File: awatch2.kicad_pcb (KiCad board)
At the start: 4 copper layers, 102.4 x 46.1 mm, 167 parts, among them J101 Conn_01x02, J102 Conn_01x02, J103 Conn_01x02, J104 Conn_01x02, J301 Conn_01x02, J801 Molex 1050170001, J802 Conn_01x06, Q701 FDV301N, SW101 B3S-1000, SW102 B3S-1000, SW103 B3S-1000, SW104 B3S-1000, U1 nRF52840, U301 MAX14690, U401 W25Q128JVPIQTR, U501 BMM150, U502 APDS-9306-065, U503 BMI160, U504 BMP388, U601 SPK0641HT4H-1, U701 AYF531035 (LS013B7DH05), U801 AT93C46DN-SH-T, U802 MCP1703A-3302_SOT223, U803 FT2232HL, U901 DRV2604, X1 ABM11W-32.0000MHZ-8-B1U-T3, Y801 FH1200004

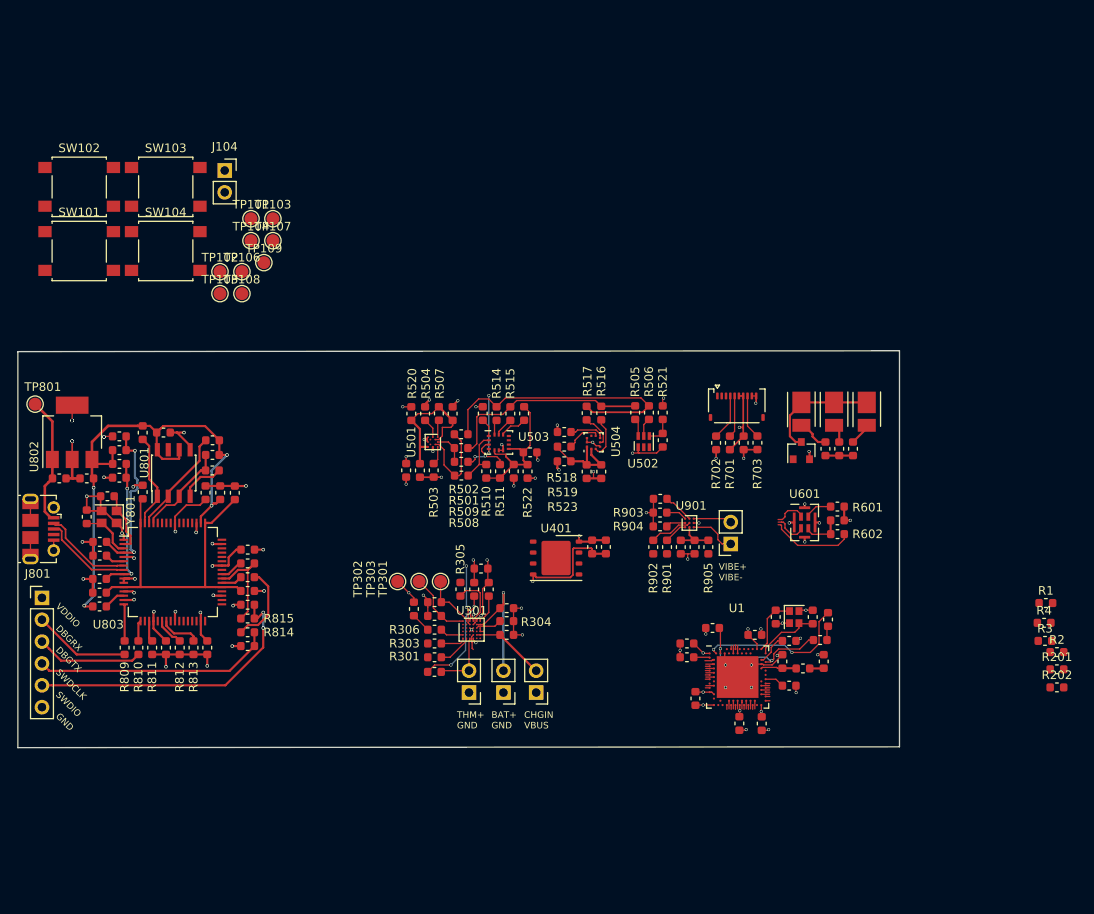
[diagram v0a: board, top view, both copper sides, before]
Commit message: place PMIC and vibrate driver
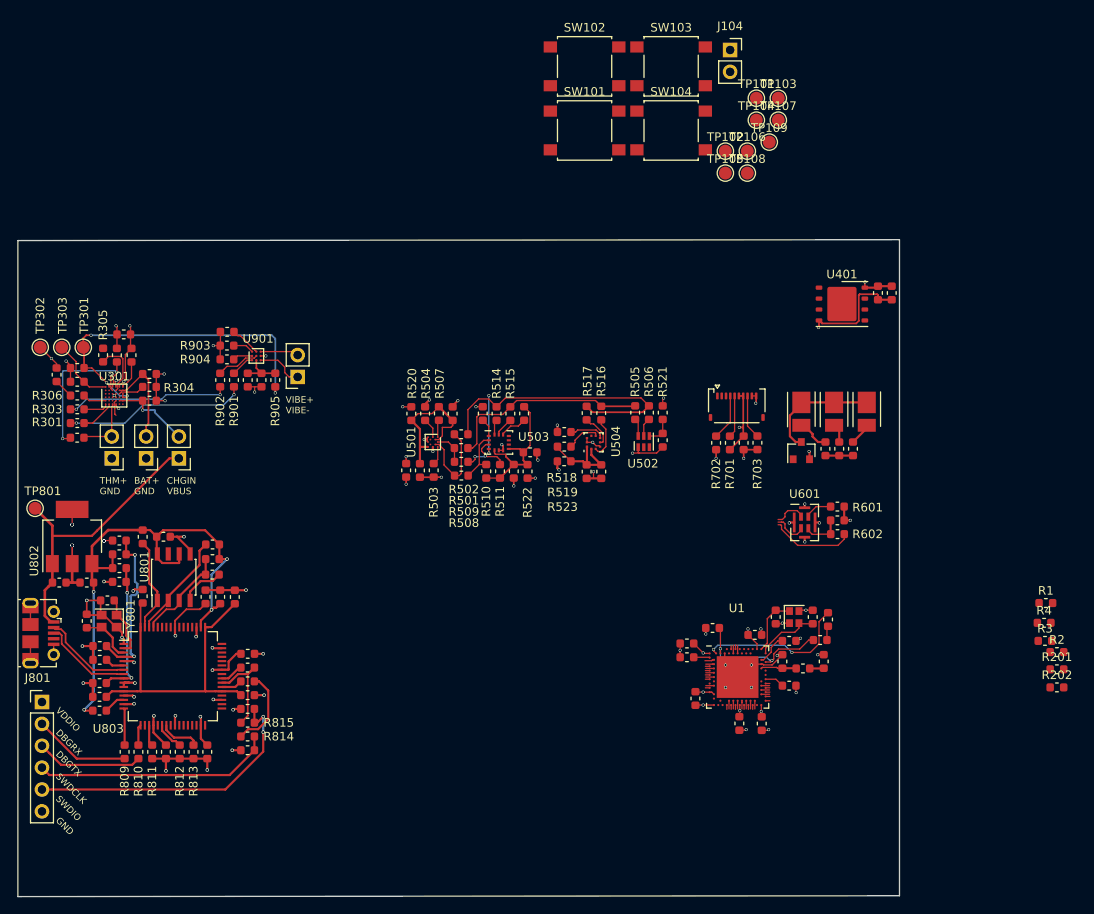
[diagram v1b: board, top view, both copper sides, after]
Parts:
- moved J104 60.3 mm to (126.7, 2.97)
- moved SW101 60.3 mm to (109.8, 12.3)
- moved SW102 60.3 mm to (109.8, 4.87)
- moved TP101 60.3 mm to (129.8, 8.57)
- moved TP104 60.3 mm to (129.8, 11.1)
- moved TP109 60.3 mm to (131.3, 13.7)
- moved SW103 60.3 mm to (119.9, 4.87)
- moved SW104 60.3 mm to (119.9, 12.3)
- moved TP102 60.3 mm to (126.2, 14.7)
- moved TP103 60.3 mm to (132.3, 8.57)
- moved TP105 60.3 mm to (126.2, 17.3)
- moved TP106 60.3 mm to (128.7, 14.7)
- moved TP107 60.3 mm to (132.3, 11.1)
- moved TP108 60.3 mm to (128.7, 17.3)
- moved R901 53.9 mm to (69.1, 41.3)
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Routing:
- net +3V8: track 7.18 -> 41.1 mm, vias 0 -> 4
- net /PMIC/PMIC_SCL: track 0.50 -> 21.8 mm, vias 0 -> 2
- net /PMIC/PMIC_SDA: track 0.95 -> 20.0 mm, vias 0 -> 2
- net VBUS: track 15.0 -> 33.4 mm
- net /PMIC/PMIC_INTn: track 7.92 -> 2.93 mm, vias 2 -> 1
- net /PMIC/MAX_CAP: track 14.1 -> 18.3 mm
- net /PMIC/BAT+: track 14.5 -> 11.7 mm, vias 1 -> 0
- net /PMIC/MAX_CHGIN: track 8.62 -> 9.46 mm, vias 0 -> 2
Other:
- board size 102.4 x 46.1 mm -> 102.4 x 76.3 mm
- net class Magnetometer 4/4: clearance 0.1016 -> 0.127
- net class NRF 3/3: clearance 0.1016 -> 0.127
- net class Vibe 2.75: clearance 0.0762 -> 0.127

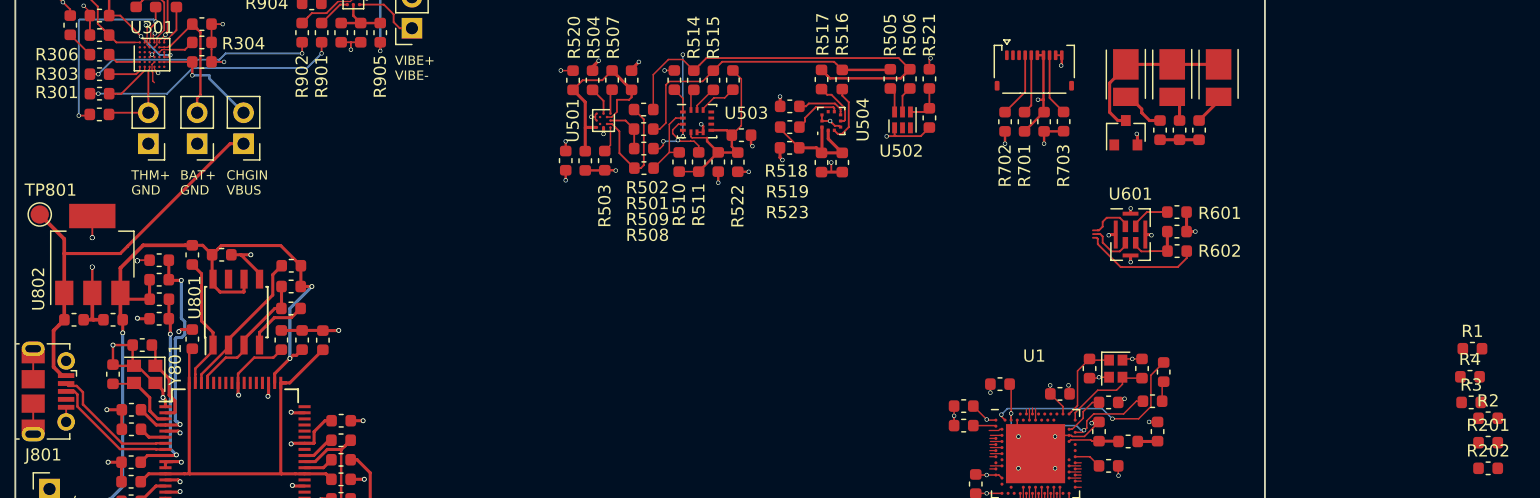
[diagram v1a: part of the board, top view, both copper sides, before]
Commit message: place PMIC I2C pullups
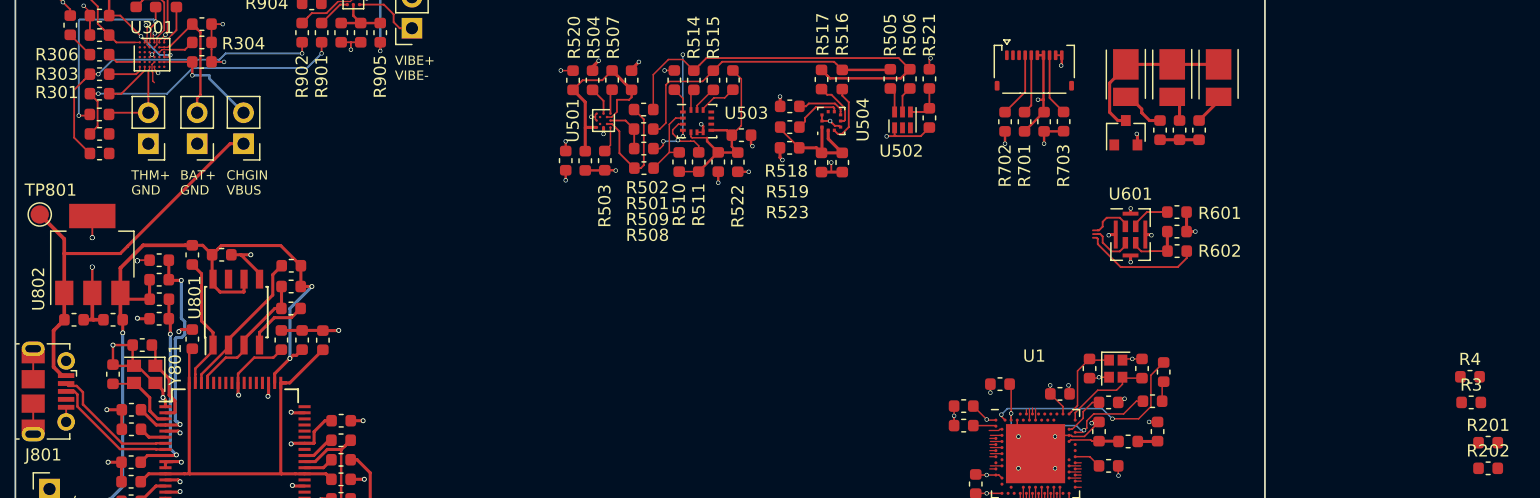
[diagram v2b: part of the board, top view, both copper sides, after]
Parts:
- moved R2 115.8 mm to (50.9, 51.2), turned to 180 degrees
- moved R1 113.9 mm to (50.9, 49.6), turned to 180 degrees
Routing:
- net /PMIC/PMIC_SDA: track 20.0 -> 27.5 mm
- net /PMIC/PMIC_SCL: track 21.8 -> 25.6 mm
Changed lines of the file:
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@@
     (thickness 1.6)
     (drawings 14)
-    (tracks 1100)
+    (tracks 1108)
     (zones 0)
     (modules 167)
@@
   )
   (module Resistor_SMD:R_0603_1608Metric (layer F.Cu)
-    (at 164.6875 72.9)
+    (at 50.9 51.2 180)
     (descr "Resistor SMD 0603 (1608 Metric), square (rectangular) end terminal, IPC_7351 nominal, (Body size source: http://www.tortai-tech.com/upload/download/2011102023233369053.pdf), generated with kicad-footprint-generator")
     (tags resistor)
     (attr smd)
-    (fp_text reference R2 (at 0 -1.43) (layer F.SilkS)
+    (fp_text reference R2 (at 0 -1.43 180) (layer F.SilkS) hide
       (effects (font (size 1 1) (thickness 0.15)))
     )
-    (fp_text value 2.2k (at 0 1.43) (layer F.Fab)
+    (fp_text value 2.2k (at 0 1.43 180) (layer F.Fab)
       (effects (font (size 1 1) (thickness 0.15)))
     )
-    (fp_text user %R (at 0 0) (layer F.Fab)
+    (fp_text user %R (at 0 0 180) (layer F.Fab)
       (effects (font (size 0.4 0.4) (thickness 0.06)))
     )
@@
     (fp_line (start -0.8 -0.4) (end 0.8 -0.4) (layer F.Fab) (width 0.1))
     (fp_line (start -0.8 0.4) (end -0.8 -0.4) (layer F.Fab) (width 0.1))
-    (pad 2 smd roundrect (at 0.7875 0) (size 0.875 0.95) (layers F.Cu F.Paste F.Mask) (roundrect_rratio 0.25)
+    (pad 2 smd roundrect (at 0.7875 0 180) (size 0.875 0.95) (layers F.Cu F.Paste F.Mask) (roundrect_rratio 0.25)
       (net 59 /PMIC/PMIC_SDA))
-    (pad 1 smd roundrect (at -0.7875 0) (size 0.875 0.95) (layers F.Cu F.Paste F.Mask) (roundrect_rratio 0.25)
+    (pad 1 smd roundrect (at -0.7875 0 180) (size 0.875 0.95) (layers F.Cu F.Paste F.Mask) (roundrect_rratio 0.25)
       (net 4 +2V8))
     (model ${KISYS3DMOD}/Resistor_SMD.3dshapes/R_0603_1608Metric.wrl
@@
   )
   (module Resistor_SMD:R_0603_1608Metric (layer F.Cu)
-    (at 163.4 67.2)
+    (at 50.9 49.6 180)
     (descr "Resistor SMD 0603 (1608 Metric), square (rectangular) end terminal, IPC_7351 nominal, (Body size source: http://www.tortai-tech.com/upload/download/2011102023233369053.pdf), generated with kicad-footprint-generator")
     (tags resistor)
     (attr smd)
-    (fp_text reference R1 (at 0 -1.43) (layer F.SilkS)
+    (fp_text reference R1 (at 0 -1.43 180) (layer F.SilkS) hide
       (effects (font (size 1 1) (thickness 0.15)))
     )
-    (fp_text value 2.2k (at 0 1.43) (layer F.Fab)
+    (fp_text value 2.2k (at 0 1.43 180) (layer F.Fab)
       (effects (font (size 1 1) (thickness 0.15)))
     )
@@
     (fp_line (start 1.48 -0.73) (end 1.48 0.73) (layer F.CrtYd) (width 0.05))
     (fp_line (start 1.48 0.73) (end -1.48 0.73) (layer F.CrtYd) (width 0.05))
-    (fp_text user %R (at 0 0) (layer F.Fab)
+    (fp_text user %R (at 0 0 180) (layer F.Fab)
       (effects (font (size 0.4 0.4) (thickness 0.06)))
     )
-    (pad 1 smd roundrect (at -0.7875 0) (size 0.875 0.95) (layers F.Cu F.Paste F.Mask) (roundrect_rratio 0.25)
+    (pad 1 smd roundrect (at -0.7875 0 180) (size 0.875 0.95) (layers F.Cu F.Paste F.Mask) (roundrect_rratio 0.25)
       (net 4 +2V8))
-    (pad 2 smd roundrect (at 0.7875 0) (size 0.875 0.95) (layers F.Cu F.Paste F.Mask) (roundrect_rratio 0.25)
+    (pad 2 smd roundrect (at 0.7875 0 180) (size 0.875 0.95) (layers F.Cu F.Paste F.Mask) (roundrect_rratio 0.25)
       (net 60 /PMIC/PMIC_SCL))
     (model ${KISYS3DMOD}/Resistor_SMD.3dshapes/R_0603_1608Metric.wrl
@@
   (segment (start 61.236118 43) (end 67.5 43) (width 0.1524) (layer B.Cu) (net 59))
   (segment (start 67.5 43) (end 67.5 42.0875) (width 0.1524) (layer F.Cu) (net 59))
+  (segment (start 49.650888 45.161612) (end 50.1125 44.7) (width 0.1524) (layer F.Cu) (net 59))
+  (segment (start 48.818999 45.993501) (end 49.650888 45.161612) (width 0.1524) (layer F.Cu) (net 59))
+  (segment (start 48.818999 49.906499) (end 48.818999 45.993501) (width 0.1524) (layer F.Cu) (net 59))
+  (segment (start 50.1125 51.2) (end 48.818999 49.906499) (width 0.1524) (layer F.Cu) (net 59))
   (segment (start 124.35 75.05) (end 123.85 75.05) (width 0.0762) (layer F.Cu) (net 60))
   (via (at 50.8 46.3) (size 0.3556) (drill 0.254) (layers F.Cu B.Cu) (net 60))
@@
   (segment (start 58.536118 44.2) (end 67.9 44.2) (width 0.1524) (layer B.Cu) (net 60))
   (segment (start 69.1 43) (end 69.1 42.0875) (width 0.1524) (layer F.Cu) (net 60))
+  (segment (start 50.574112 46.761612) (end 50.1125 46.3) (width 0.1524) (layer F.Cu) (net 60))
+  (segment (start 50.74071 46.92821) (end 50.574112 46.761612) (width 0.1524) (layer F.Cu) (net 60))
+  (segment (start 50.74071 48.97179) (end 50.74071 46.92821) (width 0.1524) (layer F.Cu) (net 60))
+  (segment (start 50.1125 49.6) (end 50.74071 48.97179) (width 0.1524) (layer F.Cu) (net 60))
   (segment (start 71.475 79.5) (end 71.475 81.1) (width 0.254) (layer F.Cu) (net 61))
   (via (at 72.5 80.4) (size 0.4064) (drill 0.254) (layers F.Cu B.Cu) (net 61))

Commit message: Pseudofinal placement.
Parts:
- moved R201 112.0 mm to (58.8, 38.4), turned to 270 degrees
- moved J104 84.0 mm to (73.7, 68.1), turned to 180 degrees
- moved TP107 76.0 mm to (94.1, 76.8)
- moved R202 71.2 mm to (93.6, 80.3), turned to 90 degrees
- moved TP106 69.9 mm to (96.7, 76.8)
- moved TP104 66.0 mm to (92.9, 65.8)
- moved TP105 65.7 mm to (76.2, 59.9)
- moved R3 61.3 mm to (102.6, 80.2), turned to 90 degrees
- moved C4 59.6 mm to (79.5, 60.7), turned to 270 degrees
- moved TP103 59.4 mm to (93.0, 53.0), turned to 90 degrees
- moved L2 59.2 mm to (79.0, 65.5), turned to 270 degrees
- moved L3 57.9 mm to (79.9, 63.2), turned to 180 degrees
- moved TP109 57.3 mm to (87.0, 50.0)
- moved SW104 56.4 mm to (108.5, 67.6)
- moved SW103 56.3 mm to (108.5, 60.0)
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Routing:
- net GND: track 158.2 -> 190.0 mm, vias 80 -> 84
- net /nRF52840/BTN_UP: track 0.50 -> 8.45 mm
- net /nRF52840/BTN_DOWN: track 0.50 -> 8.45 mm
- net /nRF52840/BTN_CENTER: track 0.95 -> 8.90 mm
- net /PMIC/BTN_BACK: track 2.82 -> 10.8 mm
- net /PMIC/PMIC_INTn: track 2.93 -> 9.33 mm, vias 1 -> 2
- net /Sensors/SENS_SDA: track 33.9 -> 39.7 mm
- net +2V8: track 57.0 -> 61.6 mm, vias 20 -> 22
- net /nRF52840/NRF_ANT: track 1.64 -> 4.95 mm
- net /Sensors/SENS_IMU_INT: track 7.70 -> 10.8 mm
- net /Sensors/SENS_SCL: track 24.3 -> 26.8 mm, vias 0 -> 2
- net Net-(C15-Pad2): track 17.1 -> 16.2 mm
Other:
- board size 102.4 x 76.3 mm -> 73.4 x 64.4 mm
- board text added: "Asterix BigBoard A00"
- board text added: "SSUART TX/RX"

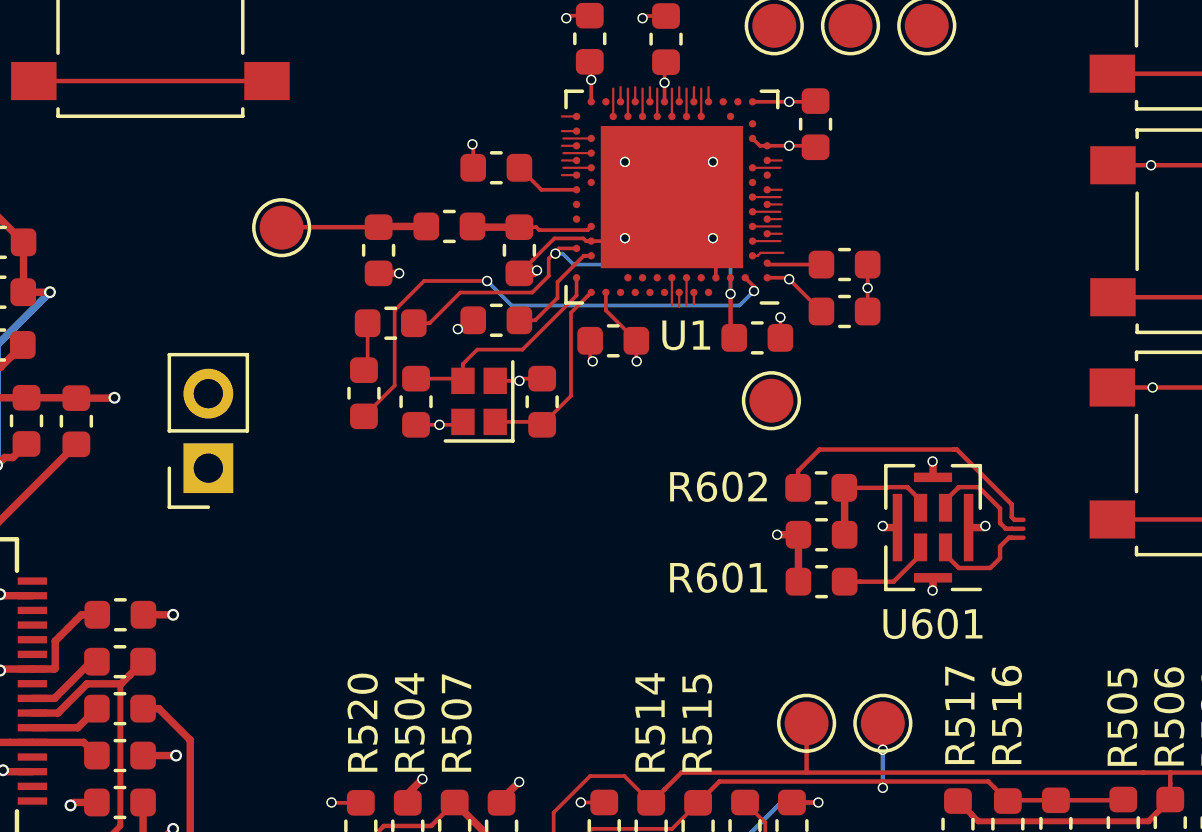
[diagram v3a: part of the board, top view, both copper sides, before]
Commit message: route NFC
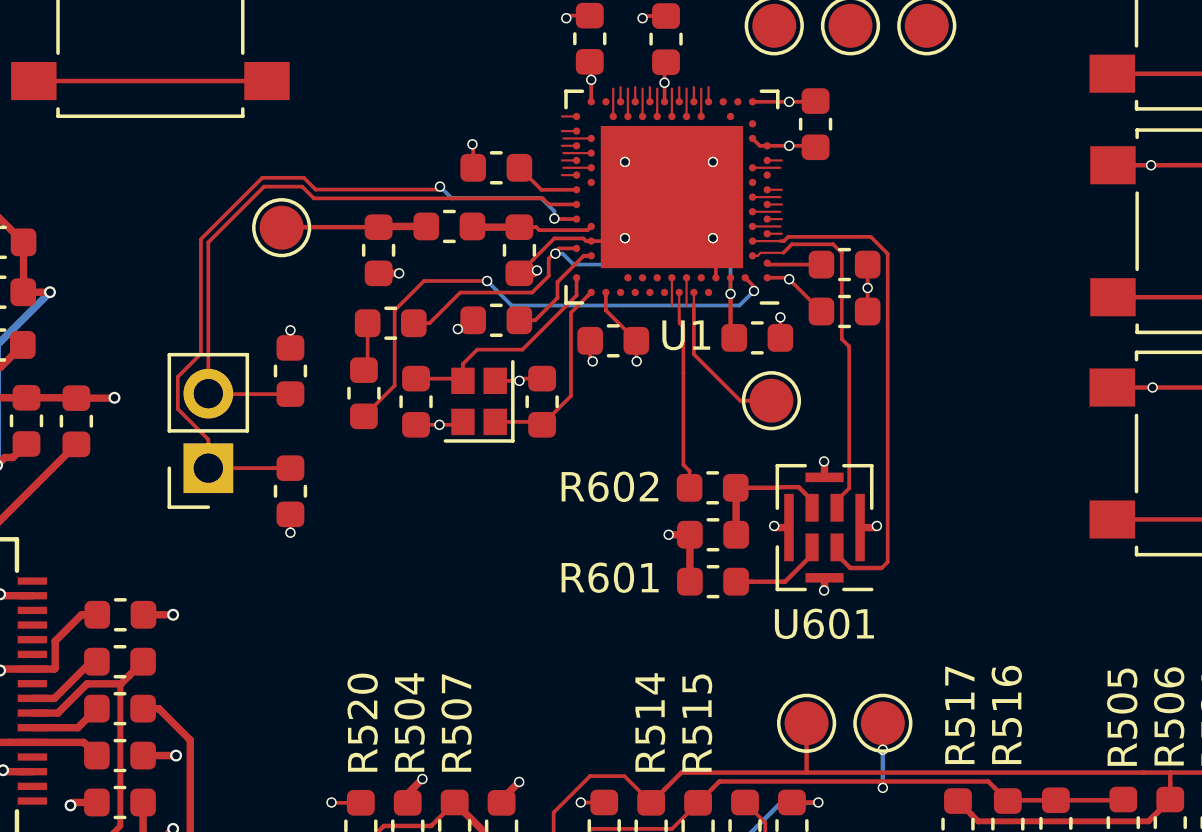
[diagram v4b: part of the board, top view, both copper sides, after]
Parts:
- added C201: ?pF NP0, Capacitor_SMD:C_0603_1608Metric, F.Cu at (76.5, 64.8)
- added C202: ?pF NP0, Capacitor_SMD:C_0603_1608Metric, F.Cu at (76.5, 68.9)
- moved C601 3.70 mm to (90.9, 70.4)
- moved R601 3.70 mm to (90.9, 72.0)
- moved R602 3.70 mm to (90.9, 68.8)
- moved U601 3.70 mm to (94.7, 70.1)
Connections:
- U1 pad D2: /Microphone/MIC_CLK -> /Microphone/MIC_DIN
- U1 pad F2: /Microphone/MIC_DIN -> /Microphone/MIC_CLK
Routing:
- net /nRF52840/NRF_NFC2: track 0.00 -> 25.9 mm, vias 0 -> 2
- net /nRF52840/NRF_NFC1: track 0.00 -> 21.6 mm
- net /Microphone/MIC_CLK: track 4.85 -> 17.7 mm
- net /Microphone/MIC_DIN: track 4.92 -> 12.3 mm
- net /nRF52840/NRF_CHICKEN3: track 0.40 -> 5.41 mm
- net /Microphone/MIC_nSTBY: track 10.3 -> 6.81 mm
- net GND: track 190.0 -> 191.2 mm, vias 84 -> 86
